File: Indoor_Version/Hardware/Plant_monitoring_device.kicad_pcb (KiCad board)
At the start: 2 copper layers, 75 x 55 mm, 67 parts, among them J1 Barrel_Jack, J10 NXW-02, J11 NXW-03, J12 NXW-03, J13 NXW-03, J14 NXW-03, J2 SWO, J3 NXW-02, J4 NXW-02, J5 NXW-02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

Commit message: Replaced STM32 with ESP32. Deleted the PCB.
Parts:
- removed A1: Antenna, MRS_Connectors:ANT_WIRE_THT
- removed BAT1: Battery, MRS_Connectors:BatteryHolder_Keystone_2468_2xAAA
- removed C13, C22: 0.1uF, MRS_Passives:C0603
- removed C21: 1uF, MRS_Passives:C0603
- removed J2: SWO, MRS_Connectors:Header_1x05_P2.54mm
- removed Q1, Q2: FDN308P, MRS_SOT:SOT-23
- removed R1, R2: 10k, MRS_Passives:R0603
- removed SB1, SB2, SB3, SB4, SB5, SB6: SolderBridge, MRS_Connectors:SB0603
- removed U2: RN2483A, MRS_Communication:RN2483A
- U1: value STM32L031K6T6 -> ESP32-WROOM; footprint MRS_QFP:LQFP-32_7x7mm_P0.8mm -> MRS_Communication:ESP32-WROOM
- moved J14 157.2 mm to (149.8, 34.8), turned to 0 degrees
- moved U4 154.4 mm to (108.8, 64.7)
- moved J13 153.3 mm to (141.0, 40.2), turned to 0 degrees
- moved C41 151.3 mm to (114.9, 65.4), turned to 0 degrees
- moved J12 151.0 mm to (141.0, 34.8), turned to 0 degrees
- moved LD6 151.0 mm to (97.9, 64.1), turned to 0 degrees
- moved J11 145.4 mm to (157.1, 23.2), turned to 0 degrees
- moved LD4 145.0 mm to (90.4, 64.1), turned to 0 degrees
- moved H1 142.5 mm to (147.6, 50.5)
- moved LD5 141.2 mm to (101.6, 64.1), turned to 0 degrees
- moved R6 135.8 mm to (111.9, 65.4), turned to 0 degrees
- moved R41 132.8 mm to (129.9, 63.9), turned to 0 degrees
- moved R42 130.2 mm to (129.9, 65.4), turned to 0 degrees
- moved LD13 129.1 mm to (94.1, 64.1), turned to 0 degrees
- moved R5 127.7 mm to (114.9, 63.9), turned to 0 degrees
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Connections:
- net /PA11 renamed Net-(U1-Pad21)
- net /PF1 renamed Net-(U1-Pad3)
- C41 pad 1: VDDA -> VCC
- J11 pad 1: VDDA -> VCC
- J12 pad 1: VDDA -> VCC
- J13 pad 1: VDDA -> VCC
- J14 pad 1: VDDA -> VCC
- Q3 pad 1: Net-(Q3-Pad1) -> /OUT1
- Q4 pad 1: Net-(Q4-Pad1) -> /OUT2
- Q5 pad 1: Net-(Q5-Pad1) -> /OUT3
- Q6 pad 1: Net-(Q6-Pad1) -> /OUT4
- R41 pad 1: VDDA -> VCC
- R42 pad 1: VDDA -> VCC
- U1 pad 1: VCC -> GND
- U1 pad 10: /ADC_SOIL4 -> Net-(U1-Pad10)
- U1 pad 11: /LED_PWM1 -> Net-(U1-Pad11)
- U1 pad 12: /LED_PWM2 -> Net-(U1-Pad12)
- U1 pad 13: /LED_PWM3 -> Net-(U1-Pad13)
- U1 pad 14: /LED_PWM4 -> Net-(U1-Pad14)
- U1 pad 15: /SENS_ENA -> Net-(U1-Pad15)
- U1 pad 16: GND -> Net-(U1-Pad16)
- U1 pad 17: VCC -> Net-(U1-Pad17)
- U1 pad 18: /BAT_LO -> Net-(U1-Pad18)
- U1 pad 19: /UART_TX -> Net-(U1-Pad19)
- U1 pad 2: /PF0 -> VCC
- U1 pad 20: /UART_RX -> Net-(U1-Pad20)
- U1 pad 22: /OUT4 -> Net-(U1-Pad22)
- U1 pad 23: /SWDIO -> Net-(U1-Pad23)
- U1 pad 24: /SWCLK -> Net-(U1-Pad24)
- U1 pad 25: /OUT3 -> Net-(U1-Pad25)
- U1 pad 26: /OUT2 -> Net-(U1-Pad26)
- U1 pad 27: /OUT1 -> Net-(U1-Pad27)
- U1 pad 28: /COMM_ENA -> Net-(U1-Pad28)
- U1 pad 29: /I2C_SCL -> Net-(U1-Pad29)
- U1 pad 30: /I2C_SDA -> Net-(U1-Pad30)
- U1 pad 31: GND -> Net-(U1-Pad31)
- U1 pad 32: GND -> Net-(U1-Pad32)
- U1 pad 4: /NRST -> Net-(U1-Pad4)
- U1 pad 5: VCC -> Net-(U1-Pad5)
- U1 pad 6: VCC -> Net-(U1-Pad6)
- U1 pad 7: /ADC_SOIL1 -> Net-(U1-Pad7)
- U1 pad 8: /ADC_SOIL2 -> Net-(U1-Pad8)
- U1 pad 9: /ADC_SOIL3 -> Net-(U1-Pad9)
- U4 pad 5: VDDA -> VCC
- U4 pad 7: VDDA -> VCC
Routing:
- net VDD: track 82.0 -> 0.00 mm
- net /LED_PWM1: track 79.3 -> 0.00 mm
- net /LED_PWM2: track 70.0 -> 0.00 mm
- net VDDA: track 68.4 -> 0.00 mm, vias 6 -> 0
- net /UART_RX: track 64.9 -> 0.00 mm, vias 2 -> 0
- net /UART_TX: track 63.8 -> 0.00 mm, vias 2 -> 0
- net /LED_PWM3: track 61.2 -> 0.00 mm
- net /LED_PWM4: track 50.6 -> 0.00 mm
- net +12V: track 48.7 -> 0.00 mm
- net /ADC_SOIL4: track 41.3 -> 0.00 mm
- net /I2C_SDA: track 38.4 -> 0.00 mm, vias 2 -> 0
- net /I2C_SCL: track 38.3 -> 0.00 mm, vias 2 -> 0
- net GND: track 33.1 -> 0.00 mm, vias 123 -> 0
- net /ADC_SOIL3: track 31.3 -> 0.00 mm
- net VCC: track 27.4 -> 0.00 mm, vias 18 -> 0
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- removed copper zone on F.Cu, net +12V
- removed copper zone on B.Cu, net GND
- removed copper zone on F.Cu, net GND
- removed copper zone on B.Cu, net VCC
- removed copper zone on F.Cu, net VCC
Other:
- board outline removed
- board text removed: "+"
- board text removed: "-"
- board text removed: "1"
- board text removed: "2"
- board text removed: "3"
- board text removed: "4"
- board text removed: "5-24V"
- board text removed: "ANT"
- board text removed: "LED"
- board text removed: "OUT"
- board text removed: "PMD v1"
- board text removed: "SOIL 1"
- board text removed: "SOIL 2"
- board text removed: "SOIL 3"
- board text removed: "SOIL 4"

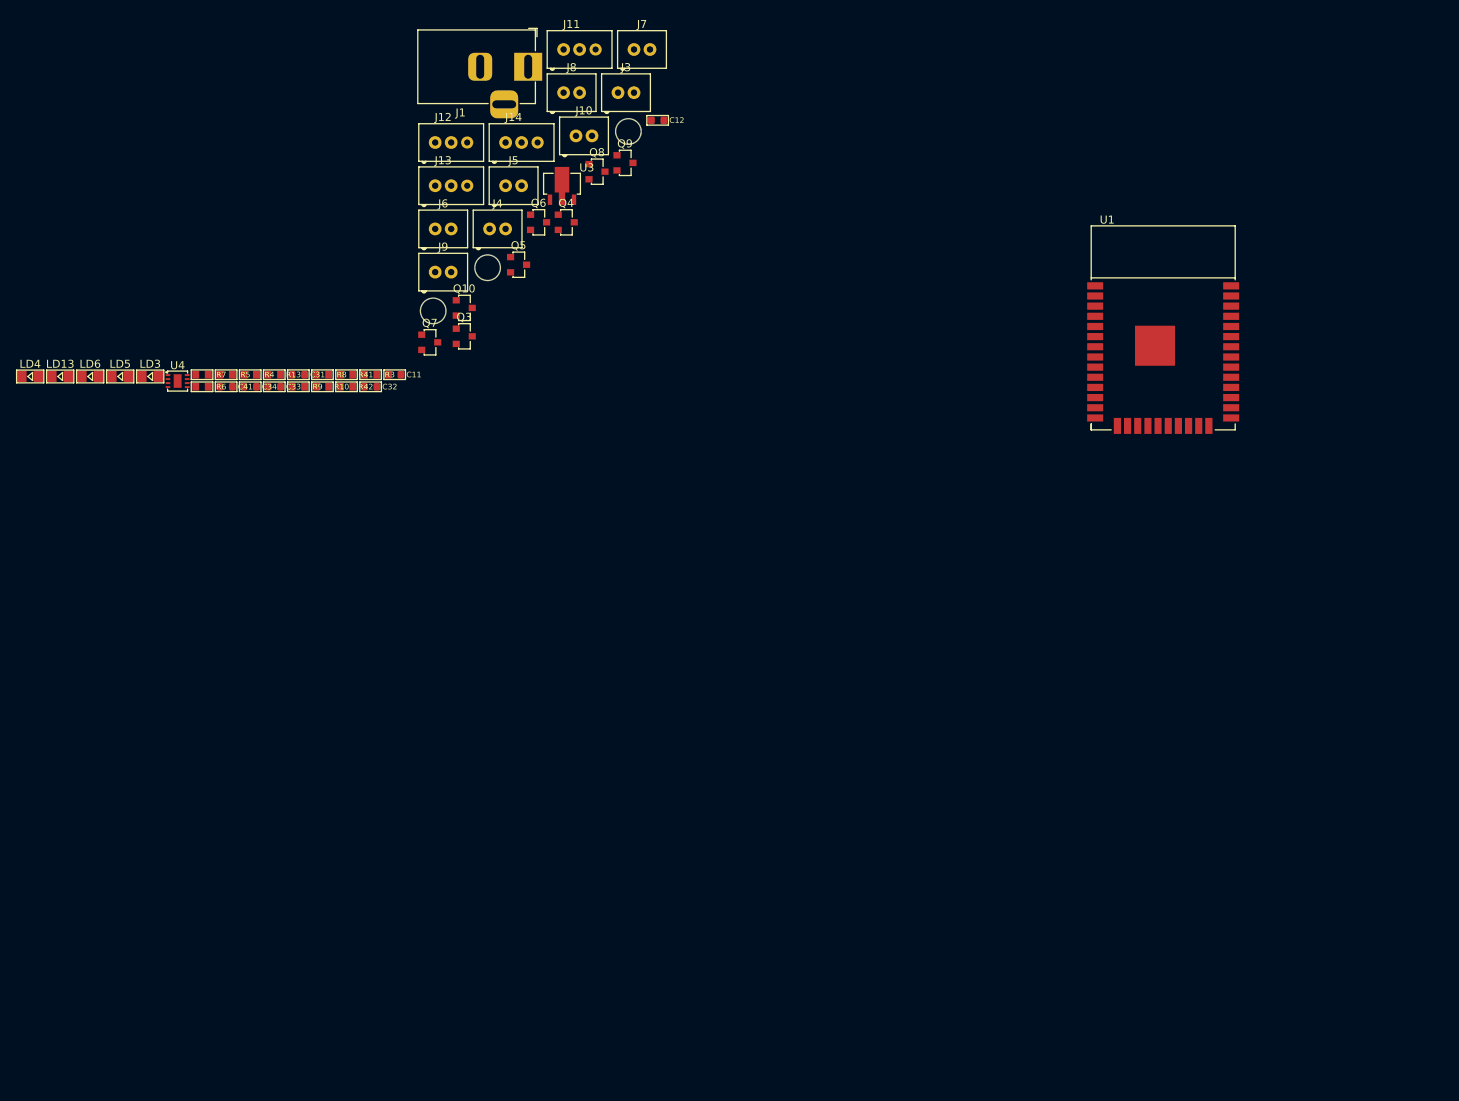
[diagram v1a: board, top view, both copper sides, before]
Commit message: Created outline of the PCB and basic layout of connectors. Created schematic and PCB layout of the buck convertor.
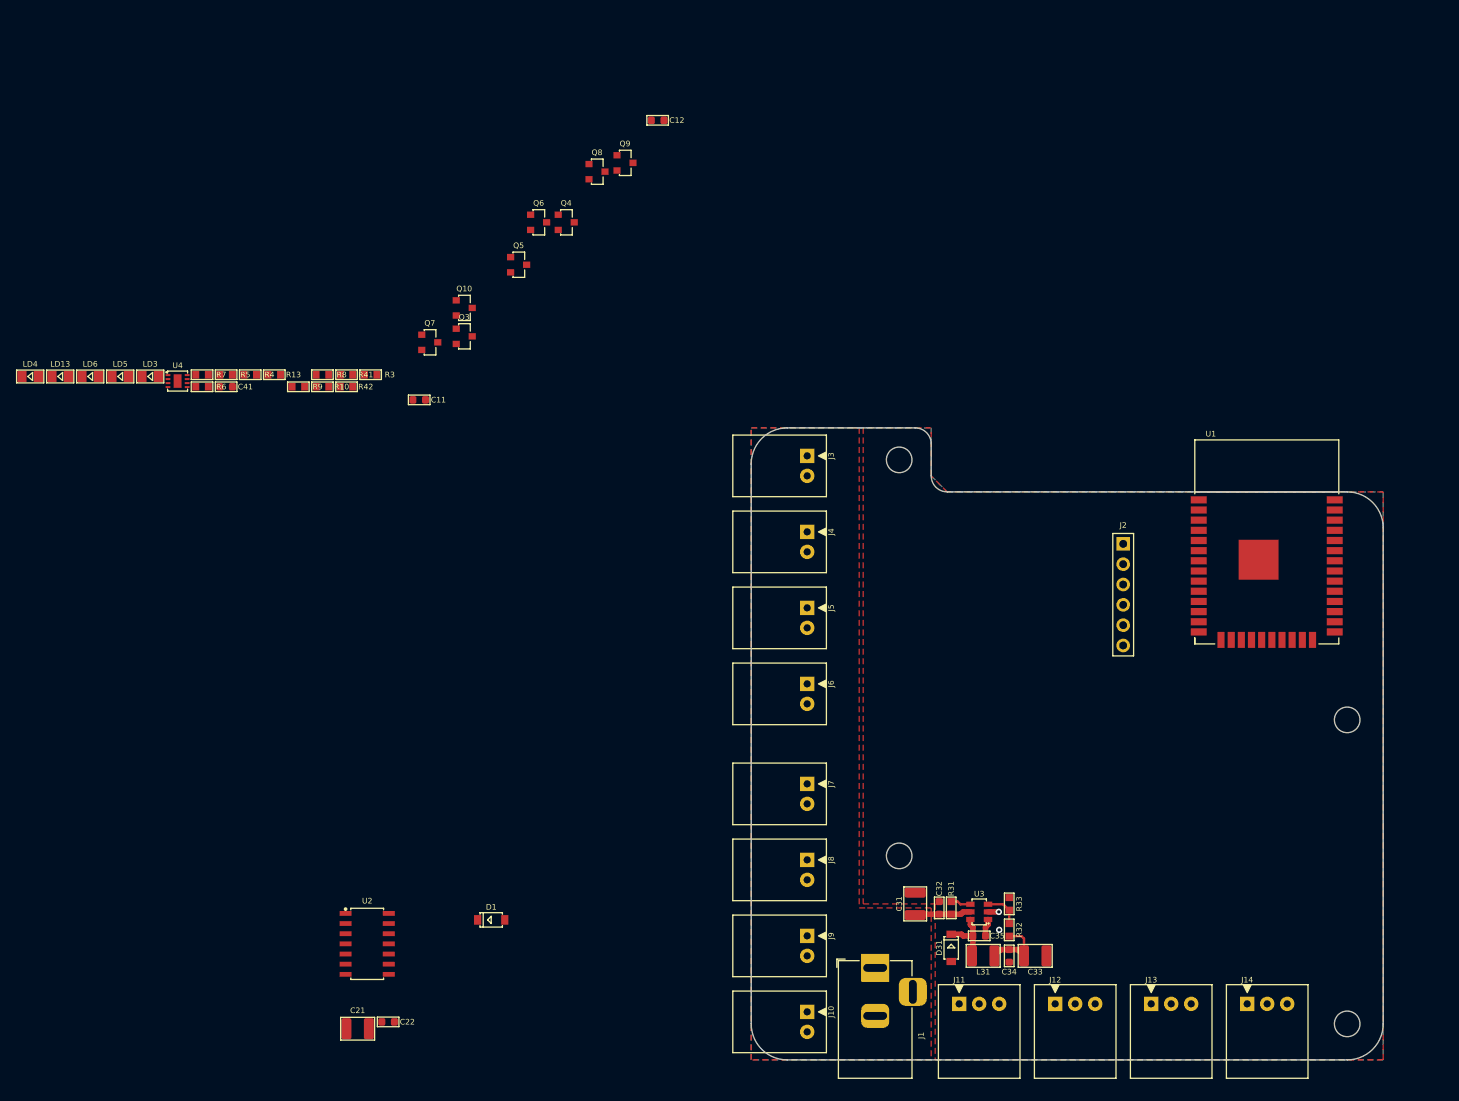
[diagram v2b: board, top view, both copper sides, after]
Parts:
- added C21: 10uF, MRS_Passives:C1210, F.Cu at (131.3, 145.6)
- added C22: 1uF, MRS_Passives:C0603, F.Cu at (135.1, 144.8)
- added C35: 10nF, MRS_Passives:C0603, F.Cu at (209.0, 134.0)
- added D1: MBR230LSFT1G, MRS_Diodes:SOD-123, F.Cu at (148.0, 132.0)
- added D31: MBR230LSFT1G, MRS_Diodes:SOD-123, F.Cu at (205.5, 135.5)
- added H4: Mounting_hole_unplated_3,2mm, MRS_Mechanical:Mounting_hole_unplated_3,2mm, F.Cu at (255.0, 107.0)
- added J2: Header_1x6, MRS_Connectors:Header_1x06_P2.54mm, F.Cu at (227.0, 85.0)
- added L31: 2.2uH, MRS_Passives:L1210, F.Cu at (209.5, 136.5)
- added R31: 10k, MRS_Passives:R0603, F.Cu at (205.5, 130.5)
- added R32: 49k9, MRS_Passives:R0603, F.Cu at (212.8, 133.2)
- added R33: 15k8, MRS_Passives:R0603, F.Cu at (212.8, 130.0)
- added U2: MCP3424-E_SL, MRS_SO:SOIC-14, F.Cu at (132.5, 135.0)
- C31, C33: footprint MRS_Passives:C0603 -> MRS_Passives:C1210
- J10, J3, J4, J5, J6, J7, J8, J9: value NXW-02 -> A2501WR-2P1; footprint MRS_Connectors:NXW-02 -> MRS_Connectors:A2501WR-2P1
- J11, J12, J13, J14: value NXW-03 -> A2501WR-3P1; footprint MRS_Connectors:NXW-03 -> MRS_Connectors:A2501WR-3P1
- U3: value AP2204RB-3.3TRG1 -> AOZ1280; footprint MRS_SOT:SOT-89 -> MRS_SOT:SOT-23-6
- moved H1 143.1 mm to (255.0, 145.0)
- moved J14 142.1 mm to (242.5, 142.5)
- moved J13 135.9 mm to (230.5, 142.5)
- moved J12 132.7 mm to (218.5, 142.5)
- moved J11 129.1 mm to (206.5, 142.5)
- moved J1 120.7 mm to (196.0, 138.0), turned to 90 degrees
- moved C33 118.8 mm to (216.0, 136.5)
- moved C34 118.6 mm to (212.8, 136.5), turned to 270 degrees
- moved J10 113.2 mm to (187.5, 143.5), turned to 270 degrees
- moved U3 104.9 mm to (209.0, 131.0), turned to 180 degrees
- moved C31 101.6 mm to (201.0, 130.0), turned to 90 degrees
- moved J8 100.6 mm to (187.5, 124.5), turned to 270 degrees
- moved H2 96.7 mm to (199.0, 124.0)
- moved C32 96.4 mm to (204.0, 130.5), turned to 90 degrees
- moved J9 95.1 mm to (187.5, 134.0), turned to 270 degrees
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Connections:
- net /BAT_LO renamed /SIG_PWM
- C11 pad 1: VCC -> +3V3
- C12 pad 1: VCC -> +3V3
- C33 pad 1: VCC -> +3V3
- C34 pad 1: VCC -> +3V3
- C41 pad 1: VCC -> +3V3
- J1 pad 1: +12V -> Net-(D1-Pad2)
- J11 pad 1: VCC -> +3V3
- J12 pad 1: VCC -> +3V3
- J13 pad 1: VCC -> +3V3
- J14 pad 1: VCC -> +3V3
- R41 pad 1: VCC -> +3V3
- R42 pad 1: VCC -> +3V3
- U1 pad 2: VCC -> +3V3
- U1 pad 25: Net-(U1-Pad25) -> /IO0
- U1 pad 3: Net-(U1-Pad3) -> /EN
- U1 pad 34: Net-(U1-Pad34) -> /UART_RX
- U1 pad 35: Net-(U1-Pad35) -> /UART_TX
- U3 pad 1: VCC -> Net-(C35-Pad1)
- U3 pad 3: +12V -> Net-(R32-Pad2)
- U4 pad 5: VCC -> +3V3
- U4 pad 7: VCC -> +3V3
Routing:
- net +3V3: track 0.00 -> 8.62 mm
- net Net-(C35-Pad2): track 0.00 -> 7.52 mm
- net +12V: track 0.00 -> 7.07 mm
- net Net-(R32-Pad2): track 0.00 -> 4.63 mm
- net Net-(R31-Pad2): track 0.00 -> 2.54 mm
- net Net-(C35-Pad1): track 0.00 -> 2.18 mm
- net GND: track 0.00 -> 1.35 mm, vias 0 -> 2
- added copper zone on F.Cu, net +12V
- added copper zone on B.Cu, net GND
- added copper zone on F.Cu, net GND
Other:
- board outline added: 79 x 79 mm
- board text added: "12V"
- board text added: "LEDS"
- board text added: "PUMPS"
- board text added: "SOIL SENSORS"
